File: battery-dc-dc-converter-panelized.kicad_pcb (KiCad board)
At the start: 2 copper layers, 110 x 129 mm, 192 parts, among them J1 Conn_01x02, J2 Conn_01x02, U1 LMR16030

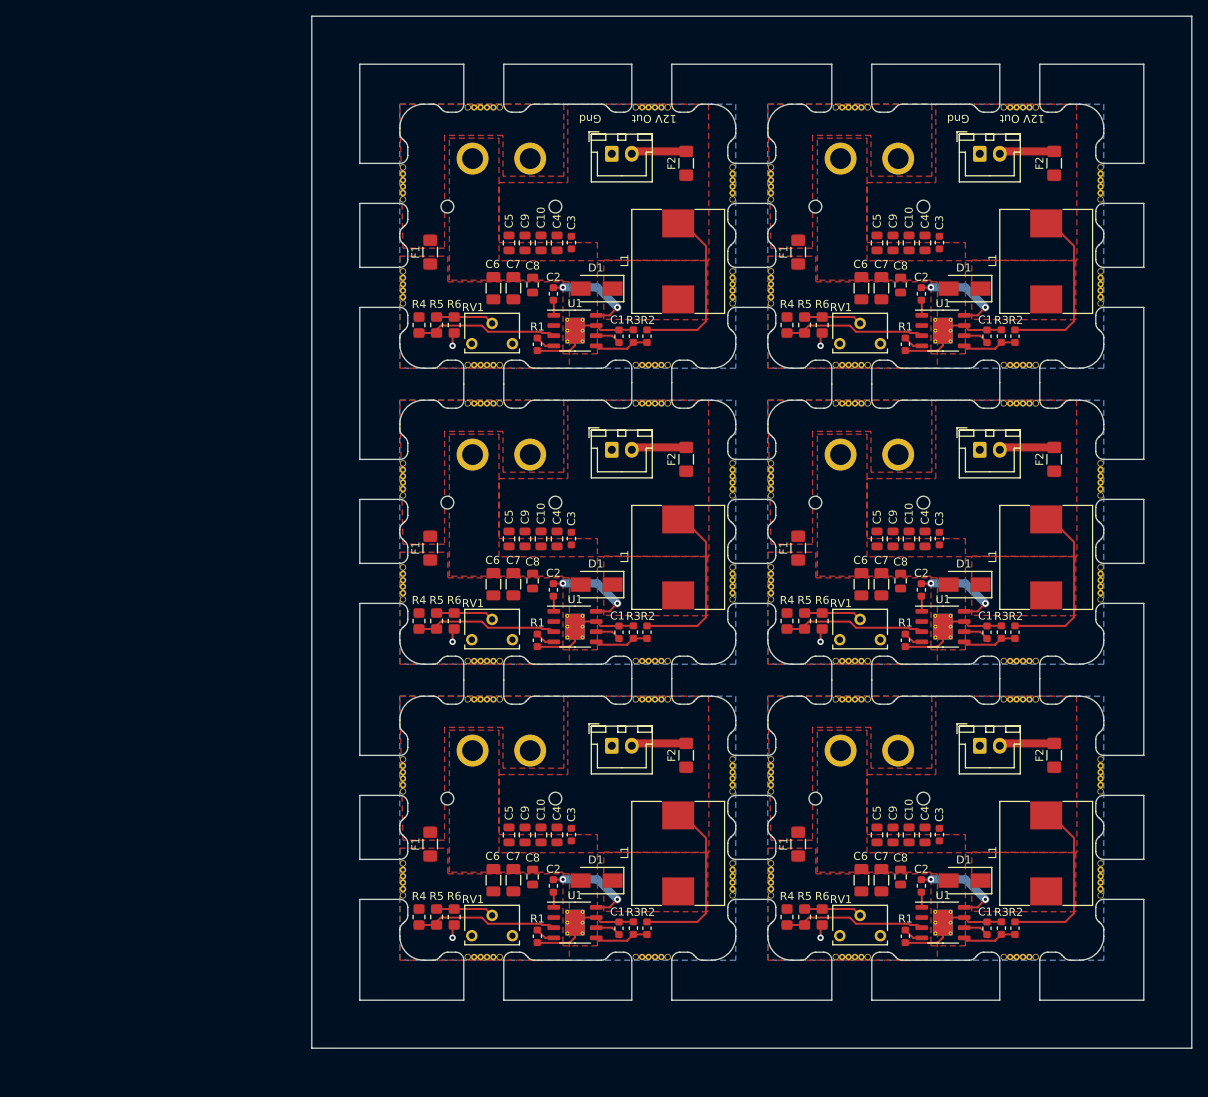
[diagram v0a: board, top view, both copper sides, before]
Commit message: Panalized PCBs
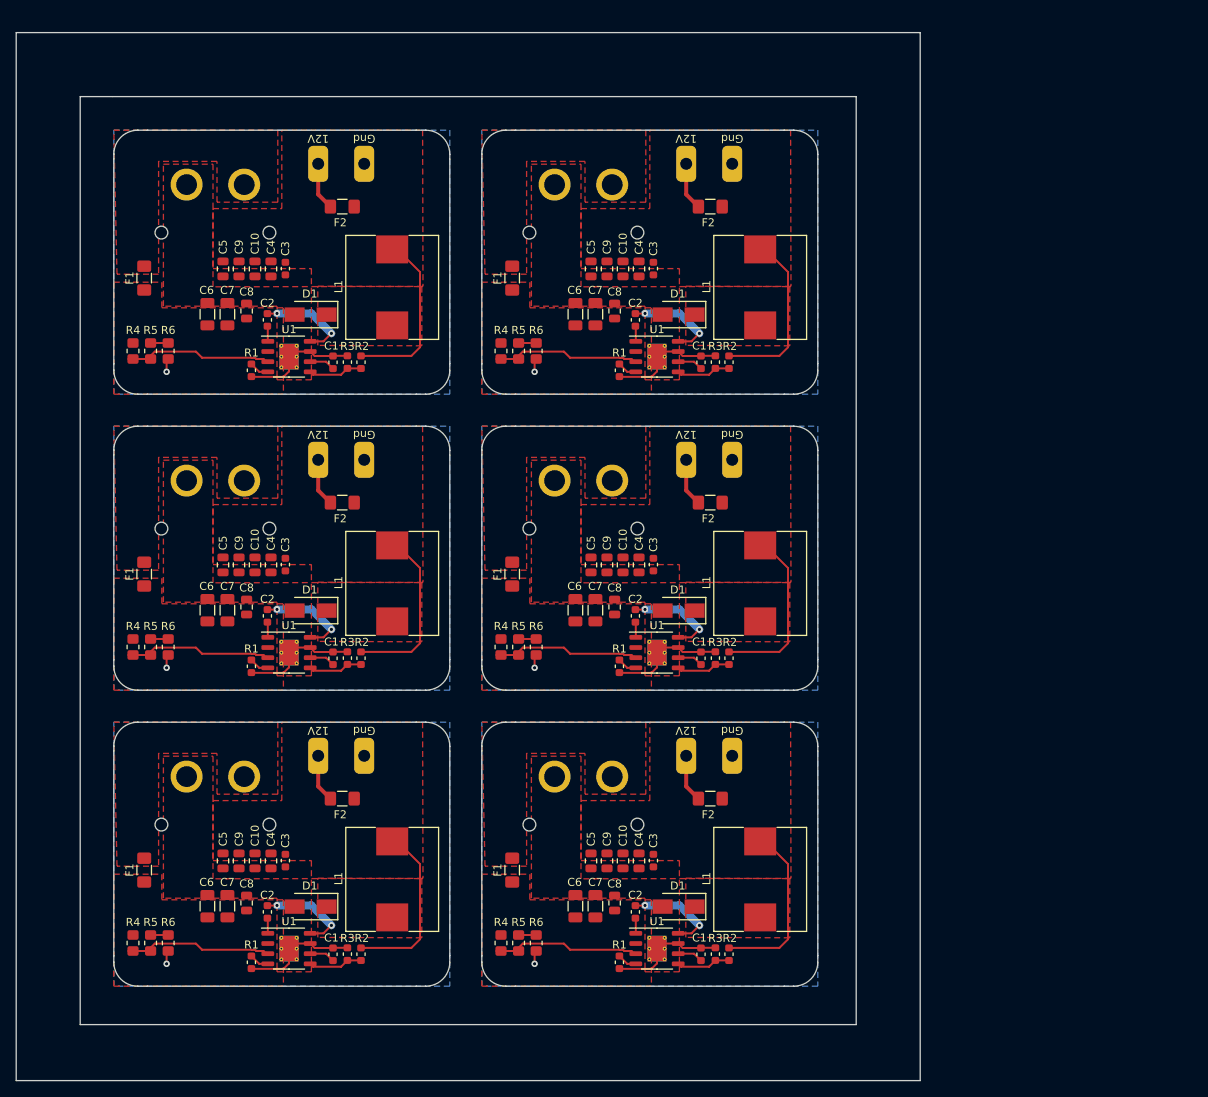
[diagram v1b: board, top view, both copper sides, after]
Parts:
- removed the C1 at (125.6, 138.2)
- removed the C1 at (171.6, 138.2)
- removed the C1 at (125.6, 101.2)
- removed the C1 at (171.6, 101.2)
- removed the C1 at (171.6, 64.2)
- removed the C10 at (115.8, 126.5)
- removed the C10 at (161.8, 126.5)
- removed the C10 at (161.8, 89.5)
- removed the C10 at (115.8, 89.5)
- removed the C10 at (161.8, 52.5)
- removed the C2 at (117.4, 132.9)
- removed the C2 at (163.4, 132.9)
- removed the C2 at (163.4, 95.9)
- removed the C2 at (117.4, 95.9)
- removed the C2 at (163.4, 58.9)
- removed the C3 at (165.7, 126.5)
- removed the C3 at (119.7, 126.5)
- removed the C3 at (119.7, 89.5)
- removed the C3 at (165.7, 89.5)
- removed the C3 at (165.7, 52.5)
- removed the C4 at (117.8, 126.5)
- removed the C4 at (163.8, 126.5)
- removed the C4 at (163.8, 89.5)
- removed the C4 at (117.8, 89.5)
- removed the C4 at (163.8, 52.5)
- removed the C5 at (157.8, 126.5)
- removed the C5 at (111.8, 126.5)
- removed the C5 at (111.8, 89.5)
- removed the C5 at (157.8, 89.5)
- removed the C5 at (157.8, 52.5)
- removed the C6 at (109.9, 132.2)
- removed the C6 at (155.9, 132.2)
- removed the C6 at (155.9, 95.2)
- removed the C6 at (109.9, 95.2)
- removed the C6 at (155.9, 58.2)
- removed the C7 at (112.4, 132.2)
- removed the C7 at (158.4, 132.2)
- removed the C7 at (158.4, 95.2)
- removed the C7 at (112.4, 95.2)
- removed the C7 at (158.4, 58.2)
- removed the C8 at (114.8, 131.8)
- removed the C8 at (160.8, 131.8)
- removed the C8 at (114.8, 94.8)
- removed the C8 at (160.8, 94.8)
- removed the C8 at (160.8, 57.8)
- removed the C9 at (113.8, 126.5)
- removed the C9 at (159.8, 126.5)
- removed the C9 at (159.8, 89.5)
- removed the C9 at (113.8, 89.5)
- removed the C9 at (159.8, 52.5)
- removed the D1 at (122.8, 132.2)
- removed the D1 at (168.8, 132.2)
- removed the D1 at (168.8, 95.2)
- removed the D1 at (122.8, 95.2)
- removed the D1 at (168.8, 58.2)
- removed the F1 at (102.0, 127.7)
- removed the F1 at (148.0, 127.7)
- removed the F1 at (148.0, 90.7)
- removed the F1 at (102.0, 90.7)
- removed the F1 at (148.0, 53.7)
- removed the F2 at (134.0, 116.6)
- removed the F2 at (180.0, 116.6)
- removed the F2 at (180.0, 79.6)
- removed the F2 at (134.0, 79.6)
- removed the F2 at (180.0, 42.6)
- removed the J1 at (110.9, 116.0)
- removed the J1 at (156.9, 116.0)
- removed the J1 at (110.9, 79.0)
- removed the J1 at (156.9, 79.0)
- removed the J1 at (156.9, 42.0)
- removed the J2 at (124.7, 115.4)
- removed the J2 at (170.7, 115.4)
- removed the J2 at (124.7, 78.4)
- removed the J2 at (170.7, 78.4)
- removed the J2 at (170.7, 41.4)
- removed the J2 at (124.7, 41.4)
- removed the L1 at (133.0, 128.8)
- removed the L1 at (179.0, 128.8)
- removed the L1 at (133.0, 91.8)
- removed the L1 at (179.0, 91.8)
- removed the L1 at (179.0, 54.9)
- removed the R1 at (161.4, 139.2)
- removed the R1 at (115.4, 139.2)
- removed the R1 at (115.4, 102.2)
- removed the R1 at (161.4, 102.2)
- removed the R1 at (161.4, 65.2)
- removed the R2 at (129.1, 138.2)
- removed the R2 at (175.1, 138.2)
- removed the R2 at (129.1, 101.2)
- removed the R2 at (175.1, 101.2)
- removed the R2 at (175.1, 64.2)
- removed the R3 at (173.4, 138.2)
- removed the R3 at (127.4, 138.2)
- removed the R3 at (127.4, 101.2)
- removed the R3 at (173.4, 101.2)
- removed the R3 at (173.4, 64.2)
- removed the R4 at (100.6, 136.8)
- removed the R4 at (146.6, 136.8)
- removed the R4 at (146.6, 99.8)
- removed the R4 at (100.6, 99.8)
- removed the R4 at (146.6, 62.8)
- removed the R5 at (148.8, 136.8)
- removed the R5 at (102.8, 136.8)
- removed the R5 at (102.8, 99.8)
- removed the R5 at (148.8, 99.8)
- removed the R5 at (148.8, 62.8)
- removed the R6 at (151.0, 136.8)
- removed the R6 at (105.0, 136.8)
- removed the R6 at (151.0, 99.8)
- removed the R6 at (105.0, 99.8)
- removed the R6 at (151.0, 62.8)
- removed REF** (x48): mousebite, scooter-ps:mousebite
- removed RV1 (x6): 10K, Potentiometer_THT:Potentiometer_Vishay_T73XX_Horizontal
- removed the U1 at (166.1, 137.5)
- removed the U1 at (120.1, 137.5)
- removed the U1 at (166.1, 100.5)
- removed the U1 at (120.1, 100.5)
- removed the U1 at (166.1, 63.5)
- added C1: 47nF, Capacitor_SMD:C_0603_1608Metric, F.Cu at (135.8, 141.5)
- added C1: 47nF, Capacitor_SMD:C_0603_1608Metric, F.Cu at (89.8, 141.5)
- added C1: 47nF, Capacitor_SMD:C_0603_1608Metric, F.Cu at (89.8, 104.5)
- added C1: 47nF, Capacitor_SMD:C_0603_1608Metric, F.Cu at (135.8, 104.5)
- added C1: 47nF, Capacitor_SMD:C_0603_1608Metric, F.Cu at (135.8, 67.5)
- added C10: 22uF, Capacitor_SMD:C_0805_2012Metric, F.Cu at (80.1, 129.8)
- added C10: 22uF, Capacitor_SMD:C_0805_2012Metric, F.Cu at (126.1, 129.8)
- added C10: 22uF, Capacitor_SMD:C_0805_2012Metric, F.Cu at (80.1, 92.8)
- added C10: 22uF, Capacitor_SMD:C_0805_2012Metric, F.Cu at (126.1, 92.8)
- added C10: 22uF, Capacitor_SMD:C_0805_2012Metric, F.Cu at (126.1, 55.8)
- added C2: 100nF, Capacitor_SMD:C_0603_1608Metric, F.Cu at (127.7, 136.2)
- added C2: 100nF, Capacitor_SMD:C_0603_1608Metric, F.Cu at (81.7, 136.2)
- added C2: 100nF, Capacitor_SMD:C_0603_1608Metric, F.Cu at (127.7, 99.2)
- added C2: 100nF, Capacitor_SMD:C_0603_1608Metric, F.Cu at (81.7, 99.2)
- added C2: 100nF, Capacitor_SMD:C_0603_1608Metric, F.Cu at (127.7, 62.2)
- added C3: 1uF, Capacitor_SMD:C_0603_1608Metric, F.Cu at (83.9, 129.8)
- added C3: 1uF, Capacitor_SMD:C_0603_1608Metric, F.Cu at (129.9, 129.8)
- added C3: 1uF, Capacitor_SMD:C_0603_1608Metric, F.Cu at (83.9, 92.8)
- added C3: 1uF, Capacitor_SMD:C_0603_1608Metric, F.Cu at (129.9, 92.8)
- added C3: 1uF, Capacitor_SMD:C_0603_1608Metric, F.Cu at (129.9, 55.8)
- added C4: 22uF, Capacitor_SMD:C_0805_2012Metric, F.Cu at (82.1, 129.8)
- added C4: 22uF, Capacitor_SMD:C_0805_2012Metric, F.Cu at (128.1, 129.8)
- added C4: 22uF, Capacitor_SMD:C_0805_2012Metric, F.Cu at (82.1, 92.8)
- added C4: 22uF, Capacitor_SMD:C_0805_2012Metric, F.Cu at (128.1, 92.8)
- added C4: 22uF, Capacitor_SMD:C_0805_2012Metric, F.Cu at (128.1, 55.8)
- added C5: 22uF, Capacitor_SMD:C_0805_2012Metric, F.Cu at (122.1, 129.8)
- added C5: 22uF, Capacitor_SMD:C_0805_2012Metric, F.Cu at (76.1, 129.8)
- added C5: 22uF, Capacitor_SMD:C_0805_2012Metric, F.Cu at (76.1, 92.8)
- added C5: 22uF, Capacitor_SMD:C_0805_2012Metric, F.Cu at (122.1, 92.8)
- added C5: 22uF, Capacitor_SMD:C_0805_2012Metric, F.Cu at (122.1, 55.8)
- added C6: 2.2uF, Capacitor_SMD:C_1206_3216Metric, F.Cu at (74.2, 135.4)
- added C6: 2.2uF, Capacitor_SMD:C_1206_3216Metric, F.Cu at (120.2, 135.4)
- added C6: 2.2uF, Capacitor_SMD:C_1206_3216Metric, F.Cu at (74.2, 98.5)
- added C6: 2.2uF, Capacitor_SMD:C_1206_3216Metric, F.Cu at (120.2, 98.5)
- added C6: 2.2uF, Capacitor_SMD:C_1206_3216Metric, F.Cu at (120.2, 61.5)
- added C7: 2.2uF, Capacitor_SMD:C_1206_3216Metric, F.Cu at (122.7, 135.4)
- added C7: 2.2uF, Capacitor_SMD:C_1206_3216Metric, F.Cu at (76.7, 135.4)
- added C7: 2.2uF, Capacitor_SMD:C_1206_3216Metric, F.Cu at (76.7, 98.5)
- added C7: 2.2uF, Capacitor_SMD:C_1206_3216Metric, F.Cu at (122.7, 98.5)
- added C7: 2.2uF, Capacitor_SMD:C_1206_3216Metric, F.Cu at (122.7, 61.5)
- added C8: 470nF, Capacitor_SMD:C_0805_2012Metric, F.Cu at (125.0, 135.1)
- added C8: 470nF, Capacitor_SMD:C_0805_2012Metric, F.Cu at (79.0, 135.1)
- added C8: 470nF, Capacitor_SMD:C_0805_2012Metric, F.Cu at (79.0, 98.0)
- added C8: 470nF, Capacitor_SMD:C_0805_2012Metric, F.Cu at (125.0, 98.0)
- added C8: 470nF, Capacitor_SMD:C_0805_2012Metric, F.Cu at (125.0, 61.0)
- added C9: 22uF, Capacitor_SMD:C_0805_2012Metric, F.Cu at (78.1, 129.8)
- added C9: 22uF, Capacitor_SMD:C_0805_2012Metric, F.Cu at (124.1, 129.8)
- added C9: 22uF, Capacitor_SMD:C_0805_2012Metric, F.Cu at (78.1, 92.8)
- added C9: 22uF, Capacitor_SMD:C_0805_2012Metric, F.Cu at (124.1, 92.8)
- added C9: 22uF, Capacitor_SMD:C_0805_2012Metric, F.Cu at (124.1, 55.8)
- added D1: D_Shockley, Diode_SMD:D_SMA, F.Cu at (133.1, 135.5)
- added D1: D_Shockley, Diode_SMD:D_SMA, F.Cu at (87.0, 135.5)
- added D1: D_Shockley, Diode_SMD:D_SMA, F.Cu at (87.0, 98.5)
- added D1: D_Shockley, Diode_SMD:D_SMA, F.Cu at (133.1, 98.5)
- added D1: D_Shockley, Diode_SMD:D_SMA, F.Cu at (133.1, 61.5)
- added F1: 3A, Fuse:Fuse_1206_3216Metric_Pad1.42x1.75mm_HandSolder, F.Cu at (112.2, 130.9)
- added F1: 3A, Fuse:Fuse_1206_3216Metric_Pad1.42x1.75mm_HandSolder, F.Cu at (66.2, 130.9)
- added F1: 3A, Fuse:Fuse_1206_3216Metric_Pad1.42x1.75mm_HandSolder, F.Cu at (66.2, 93.9)
- added F1: 3A, Fuse:Fuse_1206_3216Metric_Pad1.42x1.75mm_HandSolder, F.Cu at (112.2, 93.9)
- added F1: 3A, Fuse:Fuse_1206_3216Metric_Pad1.42x1.75mm_HandSolder, F.Cu at (112.2, 56.9)
- added F2: 3A, Fuse:Fuse_1206_3216Metric_Pad1.42x1.75mm_HandSolder, F.Cu at (137.0, 122.0)
- added F2: 3A, Fuse:Fuse_1206_3216Metric_Pad1.42x1.75mm_HandSolder, F.Cu at (91.0, 122.0)
- added F2: 3A, Fuse:Fuse_1206_3216Metric_Pad1.42x1.75mm_HandSolder, F.Cu at (137.0, 85.0)
- added F2: 3A, Fuse:Fuse_1206_3216Metric_Pad1.42x1.75mm_HandSolder, F.Cu at (91.0, 85.0)
- added F2: 3A, Fuse:Fuse_1206_3216Metric_Pad1.42x1.75mm_HandSolder, F.Cu at (137.0, 48.0)
- added J1: Conn_01x02, scooter-ps:xt60pw-m, B.Cu at (121.2, 119.2)
- added J1: Conn_01x02, scooter-ps:xt60pw-m, B.Cu at (75.2, 119.2)
- added J1: Conn_01x02, scooter-ps:xt60pw-m, B.Cu at (121.2, 82.2)
- added J1: Conn_01x02, scooter-ps:xt60pw-m, B.Cu at (75.2, 82.2)
- added J1: Conn_01x02, scooter-ps:xt60pw-m, B.Cu at (121.2, 45.2)
- added J2: Conn_01x01, battery-dc-dc-converter:hole-pad, F.Cu at (134.0, 116.8)
- added J2: Conn_01x01, battery-dc-dc-converter:hole-pad, F.Cu at (88.0, 116.8)
- added J2: Conn_01x01, battery-dc-dc-converter:hole-pad, F.Cu at (88.0, 79.8)
- added J2: Conn_01x01, battery-dc-dc-converter:hole-pad, F.Cu at (134.0, 79.8)
- added J2: Conn_01x01, battery-dc-dc-converter:hole-pad, F.Cu at (134.0, 42.8)
- added J2: Conn_01x01, battery-dc-dc-converter:hole-pad, F.Cu at (88.0, 42.8)
- added J3: Conn_01x01, battery-dc-dc-converter:hole-pad, F.Cu at (139.8, 116.8)
- added J3: Conn_01x01, battery-dc-dc-converter:hole-pad, F.Cu at (93.8, 116.8)
- added J3: Conn_01x01, battery-dc-dc-converter:hole-pad, F.Cu at (139.8, 79.8)
- added J3: Conn_01x01, battery-dc-dc-converter:hole-pad, F.Cu at (93.8, 79.8)
- added J3: Conn_01x01, battery-dc-dc-converter:hole-pad, F.Cu at (139.8, 42.8)
- added J3: Conn_01x01, battery-dc-dc-converter:hole-pad, F.Cu at (93.8, 42.8)
- added L1: 15uH, scooter-ps:MWSA1004, F.Cu at (143.2, 132.1)
- added L1: 15uH, scooter-ps:MWSA1004, F.Cu at (97.2, 132.1)
- added L1: 15uH, scooter-ps:MWSA1004, F.Cu at (97.2, 95.1)
- added L1: 15uH, scooter-ps:MWSA1004, F.Cu at (143.2, 95.1)
- added L1: 15uH, scooter-ps:MWSA1004, F.Cu at (143.2, 58.1)
- added R1: 49K9, Resistor_SMD:R_0603_1608Metric, F.Cu at (79.7, 142.5)
- added R1: 49K9, Resistor_SMD:R_0603_1608Metric, F.Cu at (125.7, 142.5)
- added R1: 49K9, Resistor_SMD:R_0603_1608Metric, F.Cu at (79.7, 105.5)
- added R1: 49K9, Resistor_SMD:R_0603_1608Metric, F.Cu at (125.7, 105.5)
- added R1: 49K9, Resistor_SMD:R_0603_1608Metric, F.Cu at (125.7, 68.5)
- added R2: 150K, Resistor_SMD:R_0603_1608Metric, F.Cu at (139.3, 141.4)
- added R2: 150K, Resistor_SMD:R_0603_1608Metric, F.Cu at (93.3, 141.4)
- added R2: 150K, Resistor_SMD:R_0603_1608Metric, F.Cu at (93.3, 104.5)
- added R2: 150K, Resistor_SMD:R_0603_1608Metric, F.Cu at (139.3, 104.5)
- added R2: 150K, Resistor_SMD:R_0603_1608Metric, F.Cu at (139.3, 67.5)
- added R3: 10K, Resistor_SMD:R_0603_1608Metric, F.Cu at (137.7, 141.4)
- added R3: 10K, Resistor_SMD:R_0603_1608Metric, F.Cu at (91.7, 141.4)
- added R3: 10K, Resistor_SMD:R_0603_1608Metric, F.Cu at (137.7, 104.4)
- added R3: 10K, Resistor_SMD:R_0603_1608Metric, F.Cu at (91.7, 104.4)
- added R3: 10K, Resistor_SMD:R_0603_1608Metric, F.Cu at (137.7, 67.4)
- added R4: 1M, Resistor_SMD:R_0805_2012Metric_Pad1.20x1.40mm_HandSolder, F.Cu at (64.8, 140.1)
- added R4: 1M, Resistor_SMD:R_0805_2012Metric_Pad1.20x1.40mm_HandSolder, F.Cu at (110.8, 140.1)
- added R4: 1M, Resistor_SMD:R_0805_2012Metric_Pad1.20x1.40mm_HandSolder, F.Cu at (64.8, 103.0)
- added R4: 1M, Resistor_SMD:R_0805_2012Metric_Pad1.20x1.40mm_HandSolder, F.Cu at (110.8, 103.0)
- added R4: 1M, Resistor_SMD:R_0805_2012Metric_Pad1.20x1.40mm_HandSolder, F.Cu at (110.8, 66.0)
- added R5: 33K, Resistor_SMD:R_0805_2012Metric_Pad1.20x1.40mm_HandSolder, F.Cu at (113.0, 140.1)
- added R5: 33K, Resistor_SMD:R_0805_2012Metric_Pad1.20x1.40mm_HandSolder, F.Cu at (67.0, 140.1)
- added R5: 33K, Resistor_SMD:R_0805_2012Metric_Pad1.20x1.40mm_HandSolder, F.Cu at (113.0, 103.0)
- added R5: 33K, Resistor_SMD:R_0805_2012Metric_Pad1.20x1.40mm_HandSolder, F.Cu at (67.0, 103.0)
- added R5: 33K, Resistor_SMD:R_0805_2012Metric_Pad1.20x1.40mm_HandSolder, F.Cu at (113.0, 66.0)
- added R6: 3k9, Resistor_SMD:R_0805_2012Metric_Pad1.20x1.40mm_HandSolder, F.Cu at (69.2, 140.1)
- added R6: 3k9, Resistor_SMD:R_0805_2012Metric_Pad1.20x1.40mm_HandSolder, F.Cu at (115.2, 140.1)
- added R6: 3k9, Resistor_SMD:R_0805_2012Metric_Pad1.20x1.40mm_HandSolder, F.Cu at (69.2, 103.0)
- added R6: 3k9, Resistor_SMD:R_0805_2012Metric_Pad1.20x1.40mm_HandSolder, F.Cu at (115.2, 103.0)
- added R6: 3k9, Resistor_SMD:R_0805_2012Metric_Pad1.20x1.40mm_HandSolder, F.Cu at (115.2, 66.0)
- added U1: LMR16030, Package_SO:HTSOP-8-1EP_3.9x4.9mm_P1.27mm_EP2.4x3.2mm_ThermalVias, F.Cu at (84.3, 140.8)
- added U1: LMR16030, Package_SO:HTSOP-8-1EP_3.9x4.9mm_P1.27mm_EP2.4x3.2mm_ThermalVias, F.Cu at (130.3, 140.8)
- added U1: LMR16030, Package_SO:HTSOP-8-1EP_3.9x4.9mm_P1.27mm_EP2.4x3.2mm_ThermalVias, F.Cu at (84.3, 103.8)
- added U1: LMR16030, Package_SO:HTSOP-8-1EP_3.9x4.9mm_P1.27mm_EP2.4x3.2mm_ThermalVias, F.Cu at (130.3, 103.8)
- added U1: LMR16030, Package_SO:HTSOP-8-1EP_3.9x4.9mm_P1.27mm_EP2.4x3.2mm_ThermalVias, F.Cu at (130.3, 66.8)
- F1: value 1A -> 3A
- R4: value 560K -> 1M
- R5: value 18K -> 33K
- R6: value R -> 3k9
- moved F2 43.3 mm to (91.0, 48.0), turned to 0 degrees
- moved C1 35.9 mm to (89.8, 67.5)
- moved C10 35.9 mm to (80.1, 55.8)
- moved C2 35.9 mm to (81.7, 62.2)
- moved C3 35.9 mm to (83.9, 55.8)
- moved C4 35.9 mm to (82.1, 55.8)
- moved C5 35.9 mm to (76.1, 55.8)
- moved C6 35.9 mm to (74.2, 61.5)
- moved C7 35.9 mm to (76.7, 61.5)
- moved C8 35.9 mm to (79.0, 61.0)
- moved C9 35.9 mm to (78.1, 55.8)
- moved D1 35.9 mm to (87.0, 61.5)
- moved F1 35.9 mm to (66.2, 56.9)
- moved J1 35.9 mm to (75.2, 45.2)
- moved L1 35.9 mm to (97.2, 58.1)
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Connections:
- F2 pad 1: +12V -> Net-(F2-Pad1)
- F2 pad 2: Net-(F2-Pad2) -> +12V
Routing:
- net Net-(F2-Pad1): track 0.00 -> 42.5 mm
- net Net-(F2-Pad2): track 41.5 -> 0.00 mm
- net Net-(R5-Pad2): track 46.0 -> 14.4 mm
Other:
- board size 110 x 129 mm -> 113 x 131 mm
- board text added: "12V"
- board text removed: "12V Out"

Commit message: Added recessed nibbles
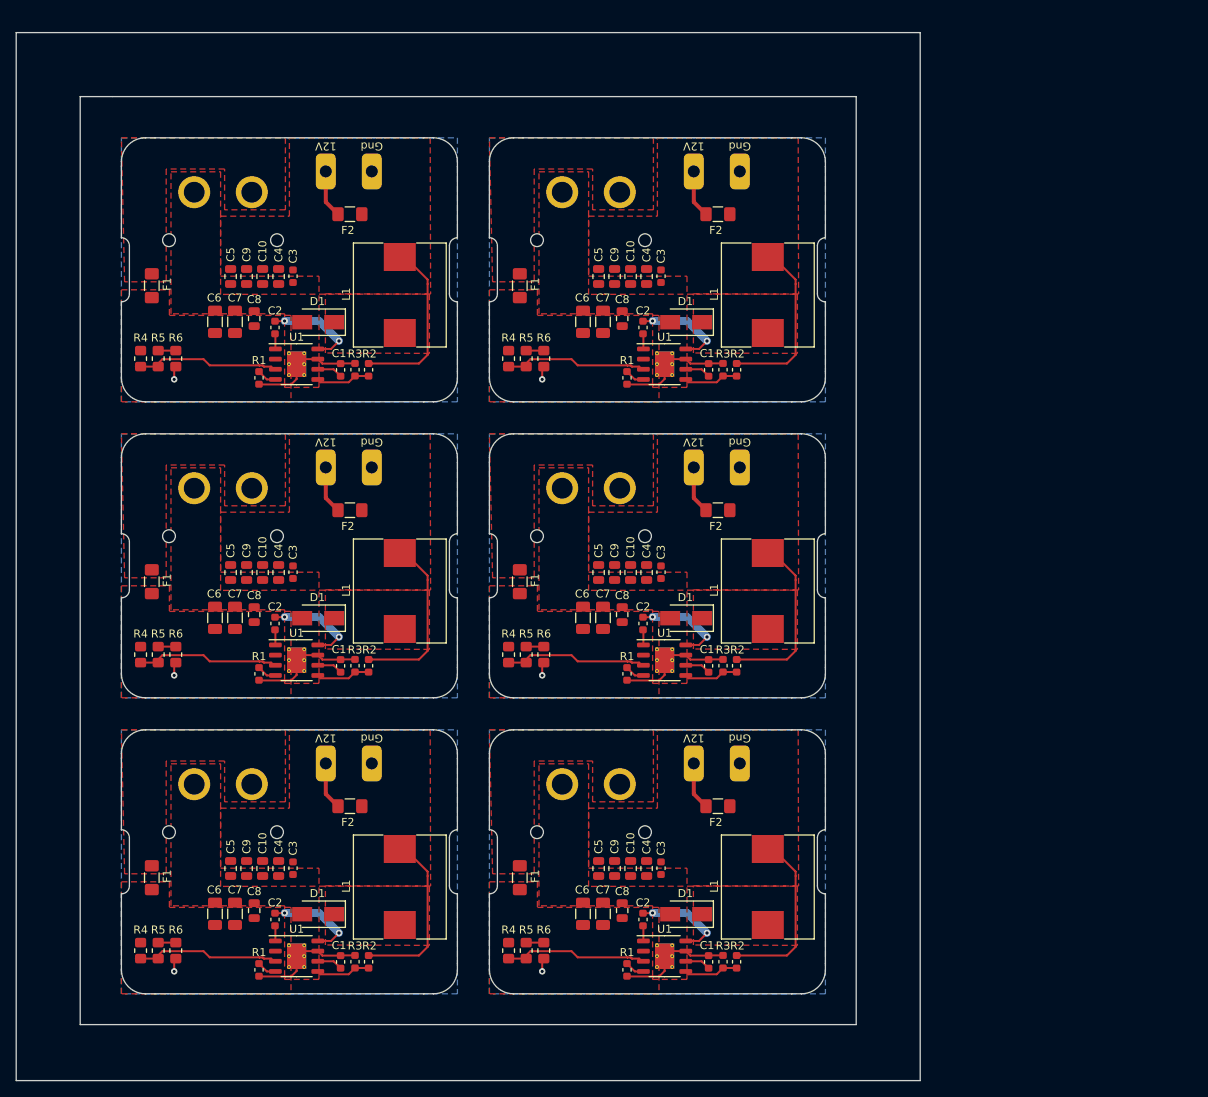
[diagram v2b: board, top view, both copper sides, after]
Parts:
- removed the C1 at (135.8, 141.5)
- removed the C1 at (89.8, 141.5)
- removed the C1 at (89.8, 104.5)
- removed the C1 at (135.8, 104.5)
- removed the C1 at (135.8, 67.5)
- removed the C10 at (80.1, 129.8)
- removed the C10 at (126.1, 129.8)
- removed the C10 at (80.1, 92.8)
- removed the C10 at (126.1, 92.8)
- removed the C10 at (126.1, 55.8)
- removed the C2 at (127.7, 136.2)
- removed the C2 at (81.7, 136.2)
- removed the C2 at (127.7, 99.2)
- removed the C2 at (81.7, 99.2)
- removed the C2 at (127.7, 62.2)
- removed the C3 at (83.9, 129.8)
- removed the C3 at (129.9, 129.8)
- removed the C3 at (83.9, 92.8)
- removed the C3 at (129.9, 92.8)
- removed the C3 at (129.9, 55.8)
- removed the C4 at (82.1, 129.8)
- removed the C4 at (128.1, 129.8)
- removed the C4 at (82.1, 92.8)
- removed the C4 at (128.1, 92.8)
- removed the C4 at (128.1, 55.8)
- removed the C5 at (122.1, 129.8)
- removed the C5 at (76.1, 129.8)
- removed the C5 at (76.1, 92.8)
- removed the C5 at (122.1, 92.8)
- removed the C5 at (122.1, 55.8)
- removed the C6 at (74.2, 135.4)
- removed the C6 at (120.2, 135.4)
- removed the C6 at (74.2, 98.5)
- removed the C6 at (120.2, 98.5)
- removed the C6 at (120.2, 61.5)
- removed the C7 at (122.7, 135.4)
- removed the C7 at (76.7, 135.4)
- removed the C7 at (76.7, 98.5)
- removed the C7 at (122.7, 98.5)
- removed the C7 at (122.7, 61.5)
- removed the C8 at (125.0, 135.1)
- removed the C8 at (79.0, 135.1)
- removed the C8 at (79.0, 98.0)
- removed the C8 at (125.0, 98.0)
- removed the C8 at (125.0, 61.0)
- removed the C9 at (78.1, 129.8)
- removed the C9 at (124.1, 129.8)
- removed the C9 at (78.1, 92.8)
- removed the C9 at (124.1, 92.8)
- removed the C9 at (124.1, 55.8)
- removed the D1 at (133.1, 135.5)
- removed the D1 at (87.0, 135.5)
- removed the D1 at (87.0, 98.5)
- removed the D1 at (133.1, 98.5)
- removed the D1 at (133.1, 61.5)
- removed the F1 at (112.2, 130.9)
- removed the F1 at (66.2, 130.9)
- removed the F1 at (66.2, 93.9)
- removed the F1 at (112.2, 93.9)
- removed the F1 at (112.2, 56.9)
- removed the F2 at (137.0, 122.0)
- removed the F2 at (91.0, 122.0)
- removed the F2 at (137.0, 85.0)
- removed the F2 at (91.0, 85.0)
- removed the F2 at (137.0, 48.0)
- removed the J1 at (121.2, 119.2)
- removed the J1 at (75.2, 119.2)
- removed the J1 at (121.2, 82.2)
- removed the J1 at (75.2, 82.2)
- removed the J1 at (121.2, 45.2)
- removed the J2 at (134.0, 116.8)
- removed the J2 at (88.0, 116.8)
- removed the J2 at (88.0, 79.8)
- removed the J2 at (134.0, 79.8)
- removed the J2 at (134.0, 42.8)
- removed the J3 at (139.8, 116.8)
- removed the J3 at (93.8, 116.8)
- removed the J3 at (139.8, 79.8)
- removed the J3 at (93.8, 79.8)
- removed the J3 at (139.8, 42.8)
- removed the L1 at (143.2, 132.1)
- removed the L1 at (97.2, 132.1)
- removed the L1 at (97.2, 95.1)
- removed the L1 at (143.2, 95.1)
- removed the L1 at (143.2, 58.1)
- removed the R1 at (79.7, 142.5)
- removed the R1 at (125.7, 142.5)
- removed the R1 at (79.7, 105.5)
- removed the R1 at (125.7, 105.5)
- removed the R1 at (125.7, 68.5)
- removed the R2 at (139.3, 141.4)
- removed the R2 at (93.3, 141.4)
- removed the R2 at (93.3, 104.5)
- removed the R2 at (139.3, 104.5)
- removed the R2 at (139.3, 67.5)
- removed the R3 at (137.7, 141.4)
- removed the R3 at (91.7, 141.4)
- removed the R3 at (137.7, 104.4)
- removed the R3 at (91.7, 104.4)
- removed the R3 at (137.7, 67.4)
- removed the R4 at (64.8, 140.1)
- removed the R4 at (110.8, 140.1)
- removed the R4 at (64.8, 103.0)
- removed the R4 at (110.8, 103.0)
- removed the R4 at (110.8, 66.0)
- removed the R5 at (113.0, 140.1)
- removed the R5 at (67.0, 140.1)
- removed the R5 at (113.0, 103.0)
- removed the R5 at (67.0, 103.0)
- removed the R5 at (113.0, 66.0)
- removed the R6 at (69.2, 140.1)
- removed the R6 at (115.2, 140.1)
- removed the R6 at (69.2, 103.0)
- removed the R6 at (115.2, 103.0)
- removed the R6 at (115.2, 66.0)
- removed the U1 at (84.3, 140.8)
- removed the U1 at (130.3, 140.8)
- removed the U1 at (84.3, 103.8)
- removed the U1 at (130.3, 103.8)
- removed the U1 at (130.3, 66.8)
- added C1: 47nF, Capacitor_SMD:C_0603_1608Metric, F.Cu at (90.8, 105.4)
- added C1: 47nF, Capacitor_SMD:C_0603_1608Metric, F.Cu at (90.8, 142.4)
- added C1: 47nF, Capacitor_SMD:C_0603_1608Metric, F.Cu at (136.8, 142.4)
- added C1: 47nF, Capacitor_SMD:C_0603_1608Metric, F.Cu at (136.8, 105.4)
- added C1: 47nF, Capacitor_SMD:C_0603_1608Metric, F.Cu at (136.8, 68.4)
- added C10: 22uF, Capacitor_SMD:C_0805_2012Metric, F.Cu at (81.0, 93.7)
- added C10: 22uF, Capacitor_SMD:C_0805_2012Metric, F.Cu at (81.0, 130.7)
- added C10: 22uF, Capacitor_SMD:C_0805_2012Metric, F.Cu at (127.0, 130.7)
- added C10: 22uF, Capacitor_SMD:C_0805_2012Metric, F.Cu at (127.0, 93.7)
- added C10: 22uF, Capacitor_SMD:C_0805_2012Metric, F.Cu at (127.0, 56.7)
- added C2: 100nF, Capacitor_SMD:C_0603_1608Metric, F.Cu at (82.6, 100.1)
- added C2: 100nF, Capacitor_SMD:C_0603_1608Metric, F.Cu at (82.6, 137.1)
- added C2: 100nF, Capacitor_SMD:C_0603_1608Metric, F.Cu at (128.6, 137.1)
- added C2: 100nF, Capacitor_SMD:C_0603_1608Metric, F.Cu at (128.6, 100.1)
- added C2: 100nF, Capacitor_SMD:C_0603_1608Metric, F.Cu at (128.6, 63.1)
- added C3: 1uF, Capacitor_SMD:C_0603_1608Metric, F.Cu at (84.8, 93.7)
- added C3: 1uF, Capacitor_SMD:C_0603_1608Metric, F.Cu at (84.8, 130.7)
- added C3: 1uF, Capacitor_SMD:C_0603_1608Metric, F.Cu at (130.8, 130.7)
- added C3: 1uF, Capacitor_SMD:C_0603_1608Metric, F.Cu at (130.8, 93.7)
- added C3: 1uF, Capacitor_SMD:C_0603_1608Metric, F.Cu at (130.8, 56.7)
- added C4: 22uF, Capacitor_SMD:C_0805_2012Metric, F.Cu at (83.0, 93.7)
- added C4: 22uF, Capacitor_SMD:C_0805_2012Metric, F.Cu at (83.0, 130.7)
- added C4: 22uF, Capacitor_SMD:C_0805_2012Metric, F.Cu at (129.1, 130.7)
- added C4: 22uF, Capacitor_SMD:C_0805_2012Metric, F.Cu at (129.1, 93.7)
- added C4: 22uF, Capacitor_SMD:C_0805_2012Metric, F.Cu at (129.1, 56.7)
- added C5: 22uF, Capacitor_SMD:C_0805_2012Metric, F.Cu at (77.0, 93.7)
- added C5: 22uF, Capacitor_SMD:C_0805_2012Metric, F.Cu at (77.0, 130.7)
- added C5: 22uF, Capacitor_SMD:C_0805_2012Metric, F.Cu at (123.0, 130.7)
- added C5: 22uF, Capacitor_SMD:C_0805_2012Metric, F.Cu at (123.0, 93.7)
- added C5: 22uF, Capacitor_SMD:C_0805_2012Metric, F.Cu at (123.0, 56.7)
- added C6: 2.2uF, Capacitor_SMD:C_1206_3216Metric, F.Cu at (75.1, 99.4)
- added C6: 2.2uF, Capacitor_SMD:C_1206_3216Metric, F.Cu at (75.1, 136.4)
- added C6: 2.2uF, Capacitor_SMD:C_1206_3216Metric, F.Cu at (121.1, 136.4)
- added C6: 2.2uF, Capacitor_SMD:C_1206_3216Metric, F.Cu at (121.1, 99.4)
- added C6: 2.2uF, Capacitor_SMD:C_1206_3216Metric, F.Cu at (121.1, 62.4)
- added C7: 2.2uF, Capacitor_SMD:C_1206_3216Metric, F.Cu at (77.6, 99.4)
- added C7: 2.2uF, Capacitor_SMD:C_1206_3216Metric, F.Cu at (77.6, 136.4)
- added C7: 2.2uF, Capacitor_SMD:C_1206_3216Metric, F.Cu at (123.6, 136.4)
- added C7: 2.2uF, Capacitor_SMD:C_1206_3216Metric, F.Cu at (123.6, 99.4)
- added C7: 2.2uF, Capacitor_SMD:C_1206_3216Metric, F.Cu at (123.6, 62.4)
- added C8: 470nF, Capacitor_SMD:C_0805_2012Metric, F.Cu at (80.0, 99.0)
- added C8: 470nF, Capacitor_SMD:C_0805_2012Metric, F.Cu at (80.0, 136.0)
- added C8: 470nF, Capacitor_SMD:C_0805_2012Metric, F.Cu at (126.0, 136.0)
- added C8: 470nF, Capacitor_SMD:C_0805_2012Metric, F.Cu at (126.0, 99.0)
- added C8: 470nF, Capacitor_SMD:C_0805_2012Metric, F.Cu at (126.0, 62.0)
- added C9: 22uF, Capacitor_SMD:C_0805_2012Metric, F.Cu at (79.0, 93.7)
- added C9: 22uF, Capacitor_SMD:C_0805_2012Metric, F.Cu at (79.0, 130.7)
- added C9: 22uF, Capacitor_SMD:C_0805_2012Metric, F.Cu at (125.0, 130.7)
- added C9: 22uF, Capacitor_SMD:C_0805_2012Metric, F.Cu at (125.0, 93.7)
- added C9: 22uF, Capacitor_SMD:C_0805_2012Metric, F.Cu at (125.0, 56.7)
- added D1: D_Shockley, Diode_SMD:D_SMA, F.Cu at (88.0, 99.5)
- added D1: D_Shockley, Diode_SMD:D_SMA, F.Cu at (88.0, 136.4)
- added D1: D_Shockley, Diode_SMD:D_SMA, F.Cu at (134.0, 136.4)
- added D1: D_Shockley, Diode_SMD:D_SMA, F.Cu at (134.0, 99.5)
- added D1: D_Shockley, Diode_SMD:D_SMA, F.Cu at (134.0, 62.5)
- added F1: 3A, Fuse:Fuse_1206_3216Metric_Pad1.42x1.75mm_HandSolder, F.Cu at (67.2, 94.9)
- added F1: 3A, Fuse:Fuse_1206_3216Metric_Pad1.42x1.75mm_HandSolder, F.Cu at (67.2, 131.9)
- added F1: 3A, Fuse:Fuse_1206_3216Metric_Pad1.42x1.75mm_HandSolder, F.Cu at (113.2, 131.9)
- added F1: 3A, Fuse:Fuse_1206_3216Metric_Pad1.42x1.75mm_HandSolder, F.Cu at (113.2, 94.9)
- added F1: 3A, Fuse:Fuse_1206_3216Metric_Pad1.42x1.75mm_HandSolder, F.Cu at (113.2, 57.9)
- added F2: 3A, Fuse:Fuse_1206_3216Metric_Pad1.42x1.75mm_HandSolder, F.Cu at (92.0, 86.0)
- added F2: 3A, Fuse:Fuse_1206_3216Metric_Pad1.42x1.75mm_HandSolder, F.Cu at (92.0, 123.0)
- added F2: 3A, Fuse:Fuse_1206_3216Metric_Pad1.42x1.75mm_HandSolder, F.Cu at (138.0, 123.0)
- added F2: 3A, Fuse:Fuse_1206_3216Metric_Pad1.42x1.75mm_HandSolder, F.Cu at (138.0, 86.0)
- added F2: 3A, Fuse:Fuse_1206_3216Metric_Pad1.42x1.75mm_HandSolder, F.Cu at (138.0, 49.0)
- added J1: Conn_01x02, scooter-ps:xt60pw-m, B.Cu at (76.1, 83.2)
- added J1: Conn_01x02, scooter-ps:xt60pw-m, B.Cu at (76.1, 120.2)
- added J1: Conn_01x02, scooter-ps:xt60pw-m, B.Cu at (122.1, 120.2)
- added J1: Conn_01x02, scooter-ps:xt60pw-m, B.Cu at (122.1, 83.2)
- added J1: Conn_01x02, scooter-ps:xt60pw-m, B.Cu at (122.1, 46.2)
- added J2: Conn_01x01, battery-dc-dc-converter:hole-pad, F.Cu at (89.0, 80.7)
- added J2: Conn_01x01, battery-dc-dc-converter:hole-pad, F.Cu at (89.0, 117.7)
- added J2: Conn_01x01, battery-dc-dc-converter:hole-pad, F.Cu at (134.9, 117.7)
- added J2: Conn_01x01, battery-dc-dc-converter:hole-pad, F.Cu at (134.9, 80.7)
- added J2: Conn_01x01, battery-dc-dc-converter:hole-pad, F.Cu at (134.9, 43.7)
- added J3: Conn_01x01, battery-dc-dc-converter:hole-pad, F.Cu at (94.7, 80.7)
- added J3: Conn_01x01, battery-dc-dc-converter:hole-pad, F.Cu at (94.7, 117.7)
- added J3: Conn_01x01, battery-dc-dc-converter:hole-pad, F.Cu at (140.7, 117.7)
- added J3: Conn_01x01, battery-dc-dc-converter:hole-pad, F.Cu at (140.7, 80.7)
- added J3: Conn_01x01, battery-dc-dc-converter:hole-pad, F.Cu at (140.7, 43.7)
- added L1: 15uH, scooter-ps:MWSA1004, F.Cu at (98.2, 96.0)
- added L1: 15uH, scooter-ps:MWSA1004, F.Cu at (98.2, 133.1)
- added L1: 15uH, scooter-ps:MWSA1004, F.Cu at (144.2, 133.1)
- added L1: 15uH, scooter-ps:MWSA1004, F.Cu at (144.2, 96.0)
- added L1: 15uH, scooter-ps:MWSA1004, F.Cu at (144.2, 59.0)
- added R1: 49K9, Resistor_SMD:R_0603_1608Metric, F.Cu at (80.6, 106.4)
- added R1: 49K9, Resistor_SMD:R_0603_1608Metric, F.Cu at (80.6, 143.4)
- added R1: 49K9, Resistor_SMD:R_0603_1608Metric, F.Cu at (126.6, 143.4)
- added R1: 49K9, Resistor_SMD:R_0603_1608Metric, F.Cu at (126.6, 106.4)
- added R1: 49K9, Resistor_SMD:R_0603_1608Metric, F.Cu at (126.6, 69.4)
- added R2: 150K, Resistor_SMD:R_0603_1608Metric, F.Cu at (94.3, 105.4)
- added R2: 150K, Resistor_SMD:R_0603_1608Metric, F.Cu at (94.3, 142.4)
- added R2: 150K, Resistor_SMD:R_0603_1608Metric, F.Cu at (140.3, 142.4)
- added R2: 150K, Resistor_SMD:R_0603_1608Metric, F.Cu at (140.3, 105.4)
- added R2: 150K, Resistor_SMD:R_0603_1608Metric, F.Cu at (140.3, 68.4)
- added R3: 10K, Resistor_SMD:R_0603_1608Metric, F.Cu at (92.6, 105.4)
- added R3: 10K, Resistor_SMD:R_0603_1608Metric, F.Cu at (92.6, 142.4)
- added R3: 10K, Resistor_SMD:R_0603_1608Metric, F.Cu at (138.6, 142.4)
- added R3: 10K, Resistor_SMD:R_0603_1608Metric, F.Cu at (138.6, 105.4)
- added R3: 10K, Resistor_SMD:R_0603_1608Metric, F.Cu at (138.6, 68.4)
- added R4: 1M, Resistor_SMD:R_0805_2012Metric_Pad1.20x1.40mm_HandSolder, F.Cu at (65.8, 104.0)
- added R4: 1M, Resistor_SMD:R_0805_2012Metric_Pad1.20x1.40mm_HandSolder, F.Cu at (65.8, 141.0)
- added R4: 1M, Resistor_SMD:R_0805_2012Metric_Pad1.20x1.40mm_HandSolder, F.Cu at (111.8, 141.0)
- added R4: 1M, Resistor_SMD:R_0805_2012Metric_Pad1.20x1.40mm_HandSolder, F.Cu at (111.8, 104.0)
- added R4: 1M, Resistor_SMD:R_0805_2012Metric_Pad1.20x1.40mm_HandSolder, F.Cu at (111.8, 67.0)
- added R5: 33K, Resistor_SMD:R_0805_2012Metric_Pad1.20x1.40mm_HandSolder, F.Cu at (68.0, 104.0)
- added R5: 33K, Resistor_SMD:R_0805_2012Metric_Pad1.20x1.40mm_HandSolder, F.Cu at (68.0, 141.0)
- added R5: 33K, Resistor_SMD:R_0805_2012Metric_Pad1.20x1.40mm_HandSolder, F.Cu at (114.0, 141.0)
- added R5: 33K, Resistor_SMD:R_0805_2012Metric_Pad1.20x1.40mm_HandSolder, F.Cu at (114.0, 104.0)
- added R5: 33K, Resistor_SMD:R_0805_2012Metric_Pad1.20x1.40mm_HandSolder, F.Cu at (114.0, 67.0)
- added R6: 3k9, Resistor_SMD:R_0805_2012Metric_Pad1.20x1.40mm_HandSolder, F.Cu at (70.2, 104.0)
- added R6: 3k9, Resistor_SMD:R_0805_2012Metric_Pad1.20x1.40mm_HandSolder, F.Cu at (70.2, 141.0)
- added R6: 3k9, Resistor_SMD:R_0805_2012Metric_Pad1.20x1.40mm_HandSolder, F.Cu at (116.2, 141.0)
- added R6: 3k9, Resistor_SMD:R_0805_2012Metric_Pad1.20x1.40mm_HandSolder, F.Cu at (116.2, 104.0)
- added R6: 3k9, Resistor_SMD:R_0805_2012Metric_Pad1.20x1.40mm_HandSolder, F.Cu at (116.2, 67.0)
- added U1: LMR16030, Package_SO:HTSOP-8-1EP_3.9x4.9mm_P1.27mm_EP2.4x3.2mm_ThermalVias, F.Cu at (85.3, 104.7)
- added U1: LMR16030, Package_SO:HTSOP-8-1EP_3.9x4.9mm_P1.27mm_EP2.4x3.2mm_ThermalVias, F.Cu at (85.3, 141.7)
- added U1: LMR16030, Package_SO:HTSOP-8-1EP_3.9x4.9mm_P1.27mm_EP2.4x3.2mm_ThermalVias, F.Cu at (131.3, 141.7)
- added U1: LMR16030, Package_SO:HTSOP-8-1EP_3.9x4.9mm_P1.27mm_EP2.4x3.2mm_ThermalVias, F.Cu at (131.3, 104.7)
- added U1: LMR16030, Package_SO:HTSOP-8-1EP_3.9x4.9mm_P1.27mm_EP2.4x3.2mm_ThermalVias, F.Cu at (131.3, 67.7)
- moved C8 1.34 mm to (80.0, 62.0)
- moved D1 1.34 mm to (88.0, 62.5)
- moved F1 1.34 mm to (67.2, 57.9)
- moved F2 1.34 mm to (92.0, 49.0)
- moved J2 1.34 mm to (89.0, 43.7)
- moved J3 1.34 mm to (94.7, 43.7)
- moved R2 1.34 mm to (94.3, 68.4)
- moved R4 1.34 mm to (65.8, 67.0)
- moved R5 1.34 mm to (68.0, 67.0)
- moved R6 1.34 mm to (70.2, 67.0)
- moved U1 1.34 mm to (85.3, 67.7)
- moved C10 1.34 mm to (81.0, 56.7)
- moved C4 1.34 mm to (83.0, 56.7)
- moved C5 1.34 mm to (77.0, 56.7)
- moved C9 1.34 mm to (79.0, 56.7)
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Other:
- outline, holes or cut-outs redrawn
